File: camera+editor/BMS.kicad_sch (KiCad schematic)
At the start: 6 parts, among them J2 Jack-DC, U1 TP4056-42-ESOP8

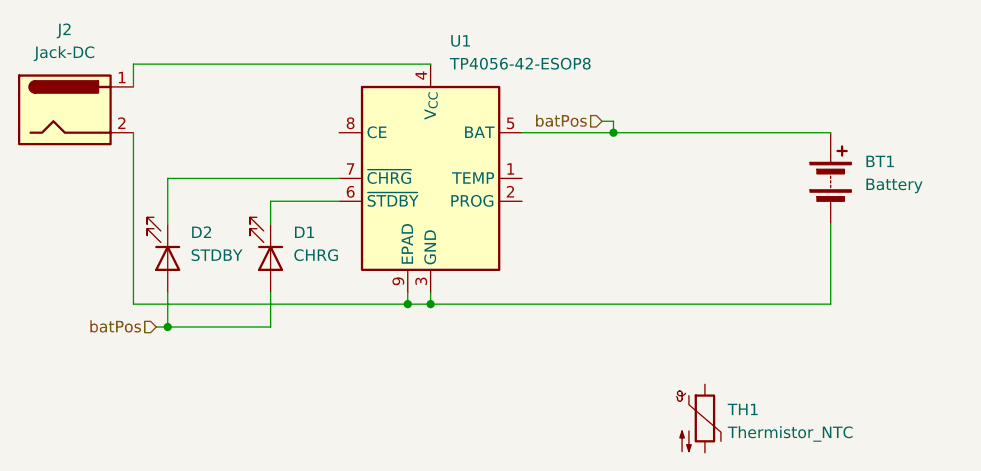
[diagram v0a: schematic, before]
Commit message: pin numbers changed inb frimware, schematic updated
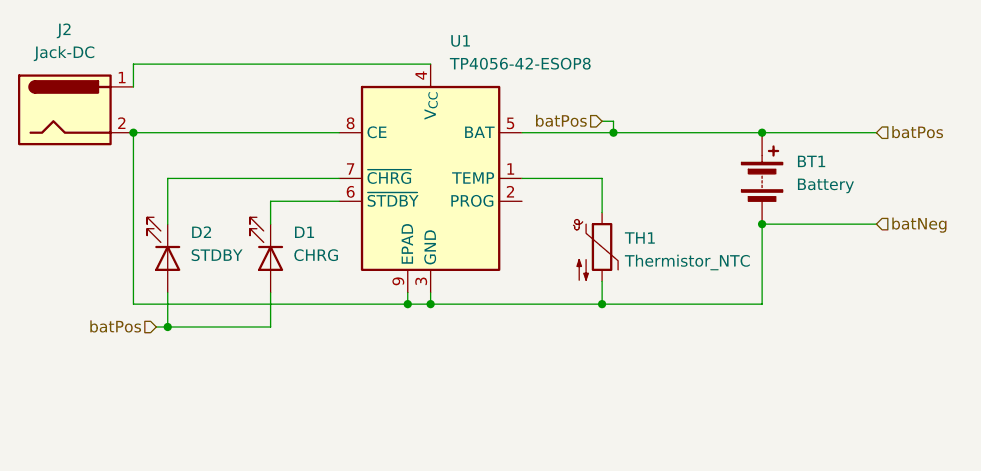
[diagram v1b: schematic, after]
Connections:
- net at TH1.1: now also U1.1 (TEMP)
- net batNeg: now reaches TH1.2
- net batNeg: now also BT1.2 (-), J2.2, U1.3 (GND), U1.8 (CE), U1.9 (EPAD)
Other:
- moved on the sheet: BT1, TH1
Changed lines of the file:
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@@
 	(paper "A4")
+	(junction
+		(at 170.18 67.31)
+		(diameter 0)
+		(color 0 0 0 0)
+	)
+	(junction
+		(at 170.18 77.47)
+		(diameter 0)
+		(color 0 0 0 0)
+	)
 	(junction
 		(at 153.67 67.31)
@@
 	)
 	(junction
+		(at 100.33 67.31)
+		(diameter 0)
+		(color 0 0 0 0)
+	)
+	(junction
+		(at 152.4 86.36)
+		(diameter 0)
+		(color 0 0 0 0)
+	)
+	(junction
 		(at 133.35 86.36)
 		(diameter 0)
@@
 	(wire
 		(pts
+			(xy 182.88 67.31) (xy 170.18 67.31)
+		)
+		(stroke
+			(width 0)
+			(type default)
+		)
+	)
+	(wire
+		(pts
 			(xy 143.51 67.31) (xy 153.67 67.31)
 		)
@@
 	(wire
 		(pts
-			(xy 177.8 86.36) (xy 177.8 77.47)
-		)
-		(stroke
-			(width 0)
-			(type default)
-		)
-	)
-	(wire
-		(pts
 			(xy 104.14 72.39) (xy 104.14 77.47)
 		)
@@
 	(wire
 		(pts
+			(xy 143.51 72.39) (xy 152.4 72.39)
+		)
+		(stroke
+			(width 0)
+			(type default)
+		)
+	)
+	(wire
+		(pts
 			(xy 115.57 85.09) (xy 115.57 88.9)
 		)
@@
 	(wire
 		(pts
-			(xy 100.33 86.36) (xy 177.8 86.36)
+			(xy 100.33 86.36) (xy 170.18 86.36)
 		)
 		(stroke
@@
 	(wire
 		(pts
+			(xy 152.4 72.39) (xy 152.4 76.2)
+		)
+		(stroke
+			(width 0)
+			(type default)
+		)
+	)
+	(wire
+		(pts
 			(xy 133.35 86.36) (xy 133.35 85.09)
 		)
@@
 	(wire
 		(pts
-			(xy 177.8 67.31) (xy 153.67 67.31)
-		)
-		(stroke
-			(width 0)
-			(type default)
-		)
-	)
-	(wire
-		(pts
 			(xy 100.33 67.31) (xy 100.33 86.36)
 		)
@@
 	(wire
 		(pts
+			(xy 100.33 67.31) (xy 123.19 67.31)
+		)
+		(stroke
+			(width 0)
+			(type default)
+		)
+	)
+	(wire
+		(pts
+			(xy 182.88 77.47) (xy 170.18 77.47)
+		)
+		(stroke
+			(width 0)
+			(type default)
+		)
+	)
+	(wire
+		(pts
+			(xy 152.4 83.82) (xy 152.4 86.36)
+		)
+		(stroke
+			(width 0)
+			(type default)
+		)
+	)
+	(wire
+		(pts
 			(xy 104.14 88.9) (xy 104.14 85.09)
+		)
+		(stroke
+			(width 0)
+			(type default)
+		)
+	)
+	(wire
+		(pts
+			(xy 170.18 86.36) (xy 170.18 77.47)
+		)
+		(stroke
+			(width 0)
+			(type default)
+		)
+	)
+	(wire
+		(pts
+			(xy 170.18 67.31) (xy 153.67 67.31)
 		)
 		(stroke
@@
 	(hierarchical_label "batPos"
 		(shape input)
+		(at 182.88 67.31 0)
+		(effects
+			(font
+				(size 1.27 1.27)
+			)
+			(justify left)
+		)
+	)
+	(hierarchical_label "batNeg"
+		(shape input)
+		(at 182.88 77.47 0)
+		(effects
+			(font
+				(size 1.27 1.27)
+			)
+			(justify left)
+		)
+	)
+	(hierarchical_label "batPos"
+		(shape input)
 		(at 152.4 66.04 180)
 		(effects
@@
 	(symbol
 		(lib_id "Device:Thermistor_NTC")
-		(at 163.83 99.06 0)
+		(at 152.4 80.01 0)
 		(unit 1)
 		(body_style 1)
@@
 		(fields_autoplaced yes)
 		(property "Reference" "TH1"
-			(at 166.37 98.1074 0)
+			(at 154.94 79.0574 0)
 			(show_name no)
 			(do_not_autoplace no)
@@
 		)
 		(property "Value" "Thermistor_NTC"
-			(at 166.37 100.6474 0)
+			(at 154.94 81.5974 0)
 			(show_name no)
 			(do_not_autoplace no)
@@
 		)
 		(property "Footprint" ""
-			(at 163.83 97.79 0)
+			(at 152.4 78.74 0)
 			(hide yes)
 			(show_name no)
@@
 		)
 		(property "Datasheet" ""
-			(at 163.83 97.79 0)
+			(at 152.4 78.74 0)
 			(hide yes)
 			(show_name no)
@@
 		)
 		(property "Description" "Temperature dependent resistor, negative temperature coefficient"
-			(at 163.83 99.06 0)
+			(at 152.4 80.01 0)
 			(hide yes)
 			(show_name no)
@@
 	(symbol
 		(lib_id "Device:Battery")
-		(at 177.8 72.39 0)
+		(at 170.18 72.39 0)
 		(unit 1)
 		(body_style 1)
@@
 		(fields_autoplaced yes)
 		(property "Reference" "BT1"
-			(at 181.61 70.5484 0)
+			(at 173.99 70.5484 0)
 			(show_name no)
 			(do_not_autoplace no)
@@
 		)
 		(property "Value" "Battery"
-			(at 181.61 73.0884 0)
+			(at 173.99 73.0884 0)
 			(show_name no)
 			(do_not_autoplace no)
@@
 		)
 		(property "Footprint" ""
-			(at 177.8 70.866 90)
+			(at 170.18 70.866 90)
 			(hide yes)
 			(show_name no)
@@
 		)
 		(property "Datasheet" ""
-			(at 177.8 70.866 90)
+			(at 170.18 70.866 90)
 			(hide yes)
 			(show_name no)
@@
 		)
 		(property "Description" "Multiple-cell battery"
-			(at 177.8 72.39 0)
+			(at 170.18 72.39 0)
 			(hide yes)
 			(show_name no)
@@
 		)
 		(property "Sim.Device" "V"
-			(at 177.8 72.39 0)
+			(at 170.18 72.39 0)
 			(hide yes)
 			(show_name no)
@@
 		)
 		(property "Sim.Type" "DC"
-			(at 177.8 72.39 0)
+			(at 170.18 72.39 0)
 			(hide yes)
 			(show_name no)
@@
 		)
 		(property "Sim.Pins" "1=+ 2=-"
-			(at 177.8 72.39 0)
-			(hide yes)
-			(show_name no)
+			(at 170.18 72.39 0)
+			(hide yes)
+			(show_name no)
